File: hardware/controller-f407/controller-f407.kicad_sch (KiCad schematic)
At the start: 0 parts

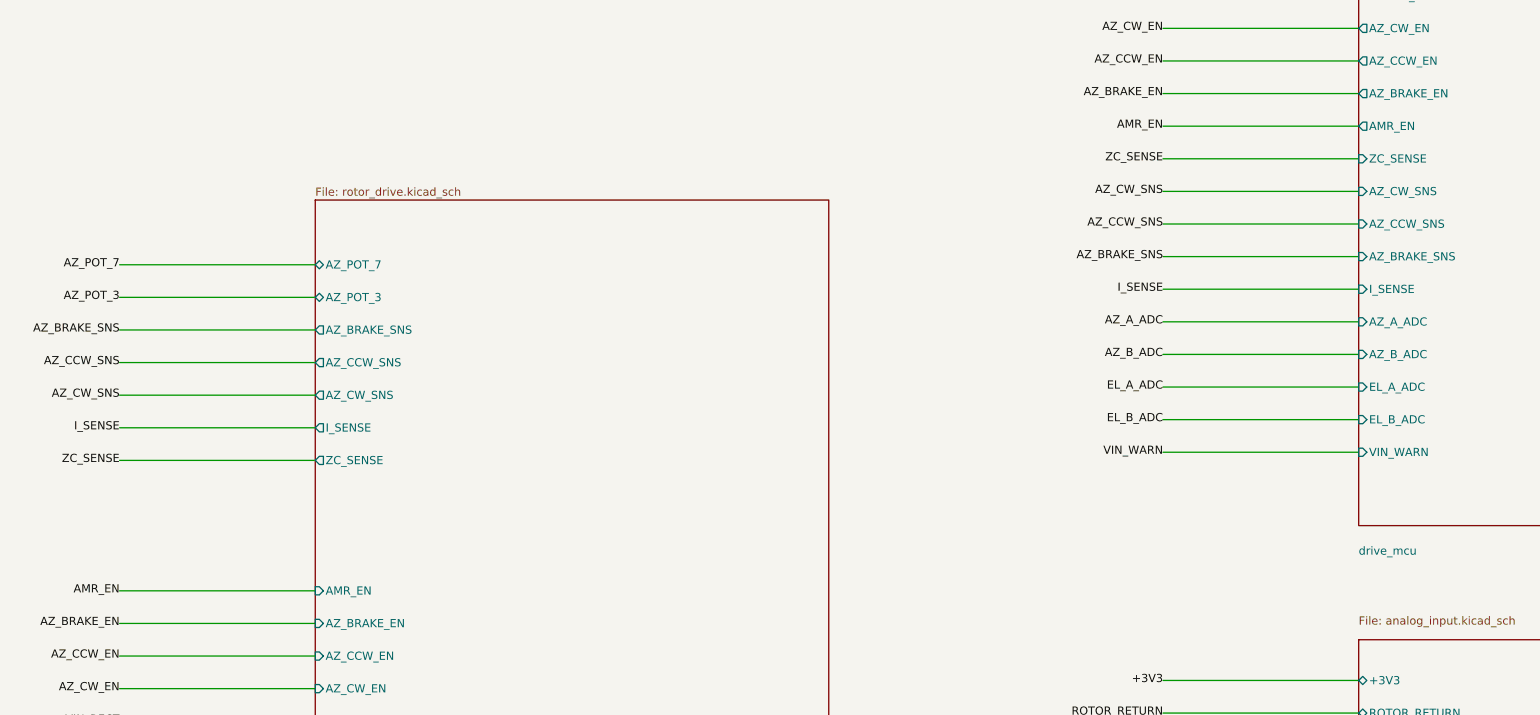
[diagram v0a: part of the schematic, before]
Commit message: Rename the relay net back to ARM_EN and drop the dangling stub.
The owner's label text is ARM_EN again, in place. One pulldown remains
on each gate line. TR1 conditioning stays on the rotor sheet.

Co-authored-by: Jeffrey Millar <wa1hco@users.noreply.github.com>
Co-authored-by: Cursor Agent <cursoragent@cursor.com>
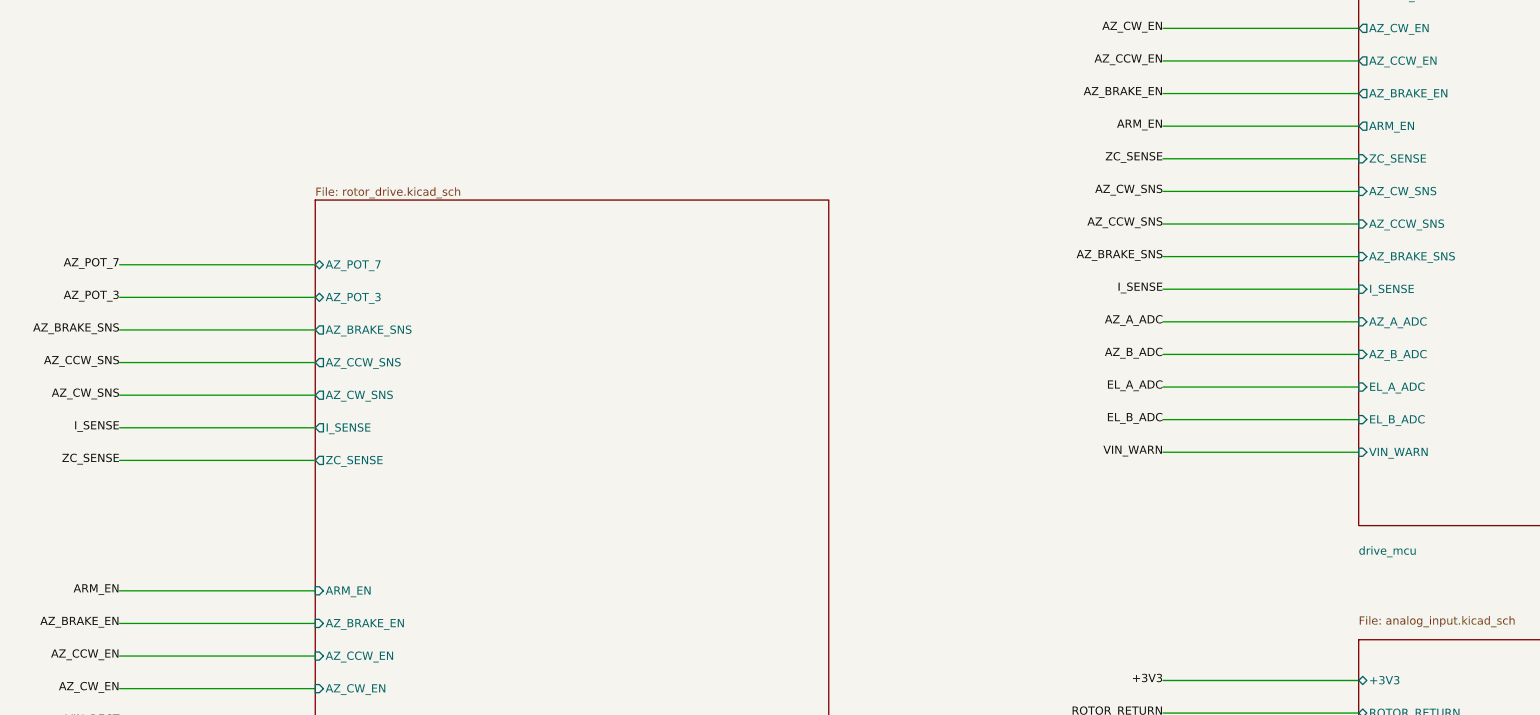
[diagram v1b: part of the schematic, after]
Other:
- sheet drive_mcu ports: added ARM_EN; removed AMR_EN
- sheet rotor_drive ports: added ARM_EN; removed AMR_EN
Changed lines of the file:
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@@
 			)
 		)
-		(pin "AMR_EN" input
+		(pin "ARM_EN" input
 			(at 86.36 116.84 180)
 			(effects
@@
 			(effects (font (size 1.27 1.27)) (justify right))
 		)
-		(pin "AMR_EN" output
+		(pin "ARM_EN" output
 			(at 248.92 44.45 180)
 			(effects (font (size 1.27 1.27)) (justify right))
@@
 	(wire (pts (xy 55.88 121.92) (xy 86.36 121.92))
 		(stroke (width 0) (type default)))
-	(label "AMR_EN" (at 55.88 116.84 180)
+	(label "ARM_EN" (at 55.88 116.84 180)
 		(effects (font (size 1.27 1.27)) (justify right))
 	)
@@
 	(wire (pts (xy 218.44 39.37) (xy 248.92 39.37))
 		(stroke (width 0) (type default)))
-	(label "AMR_EN" (at 218.44 44.45 180)
-		(effects (font (size 1.27 1.27)) (justify right))
-	)
+	(label "ARM_EN" (at 218.44 44.45 180)
+		(effects (font (size 1.27 1.27)) (justify right))
+	)
